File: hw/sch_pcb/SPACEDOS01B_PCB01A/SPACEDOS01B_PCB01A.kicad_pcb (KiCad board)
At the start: 2 copper layers, 48.2 x 93.5 mm, 92 parts, among them J1 HEADER_2x01, J19 HEADER_2x01_PARALLEL, J2 HEADER_2x01_PARALLEL, J22 HEADER_2x03, J3 HEADER_2x01_PARALLEL, J4 HEADER_1x01, J5 HEADER_1x01, J6 HEADER_1x01, J7 HEADER_1x01, M1 HOLE, M10 BMI-S-204-F, M2 HOLE, M3 HOLE, M4 HOLE, M6 BMI-S-210-F, M8 BMI-S-204-F, M9 BMI-S-204-F, U1 OPA2314, U10 ATMEGA1284P-AU, U11 PCF85263A, U2 OPA2314, U3 ISL21080DIH312Z-TK 1V25, U4 TS7211, U5 TS5A4594, U8 TPS613222ADBV, Y2 ABS07-120-32.768KHZ-T

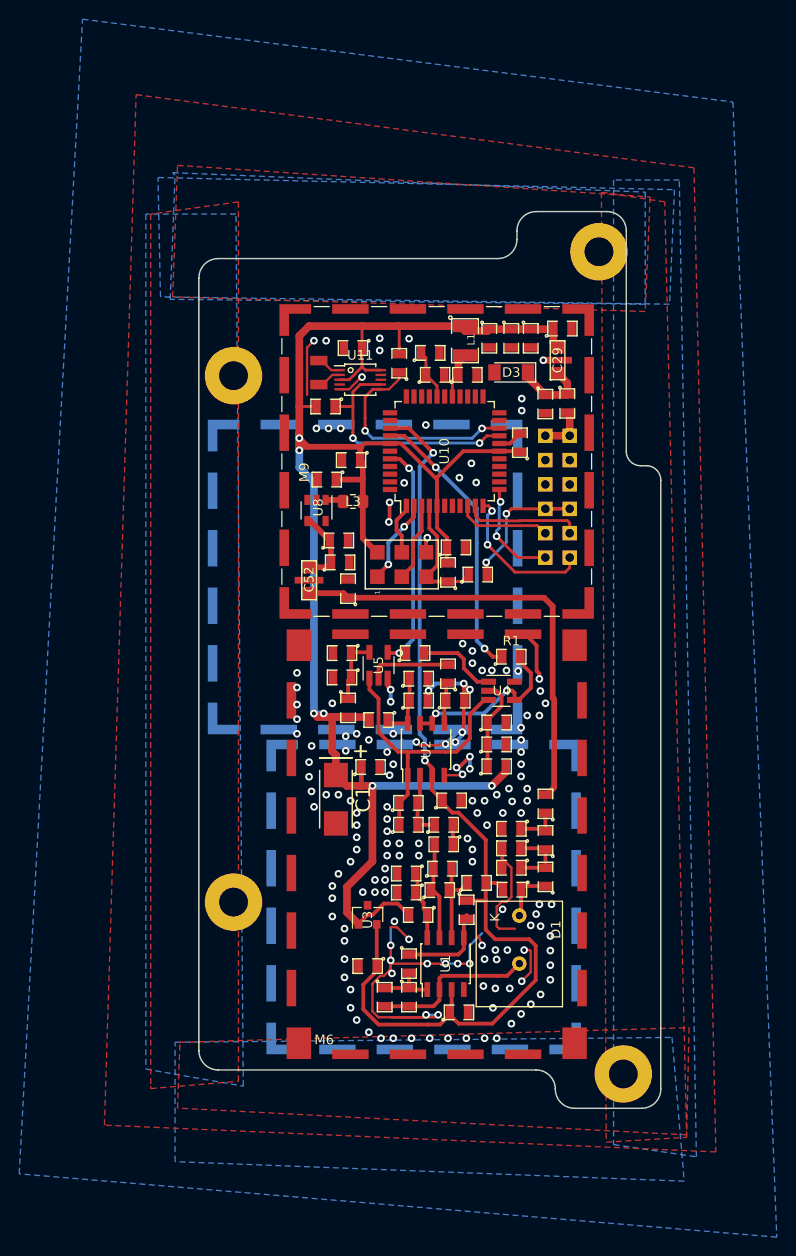
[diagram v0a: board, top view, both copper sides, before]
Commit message: Update designs to KiCAD 6. Update schematics datasheet links Minor schematics improvements (titleblocks, schematics layout)
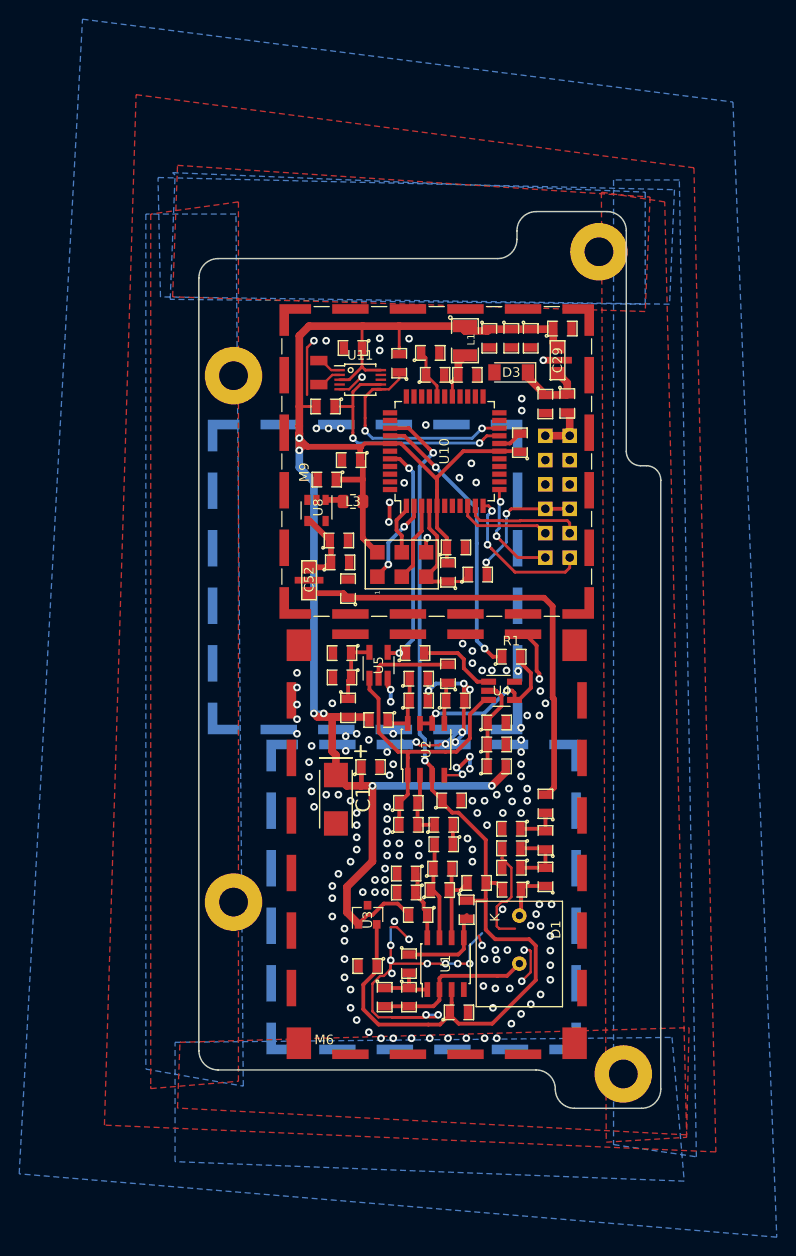
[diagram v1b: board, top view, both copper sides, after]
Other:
- net class Default removed
- net class MLAB_default removed
- net class MLAB_power removed
